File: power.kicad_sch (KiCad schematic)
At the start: 28 parts, among them Q1 CSD16340Q3, Q2 CSD17311Q5, U10 DS4432U+, U8 INA260, U9 TPS40305

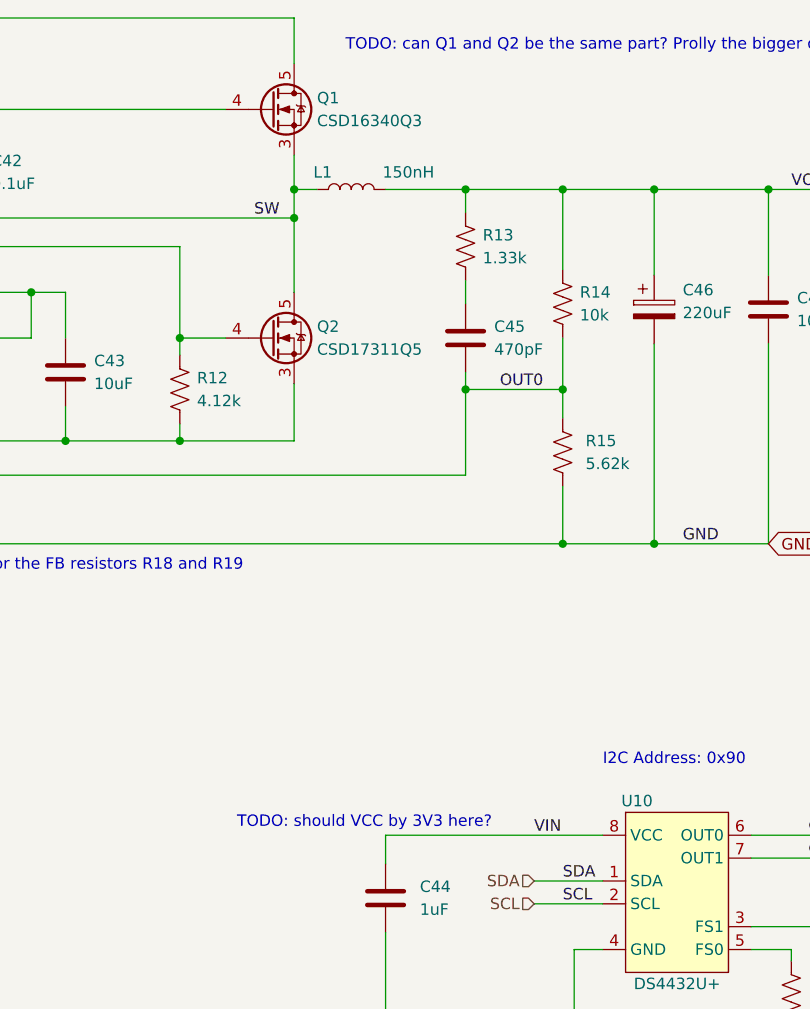
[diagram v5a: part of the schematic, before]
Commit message: schematic done, all footprints added, 3D files added. Rough placement done. needs lots of routing.
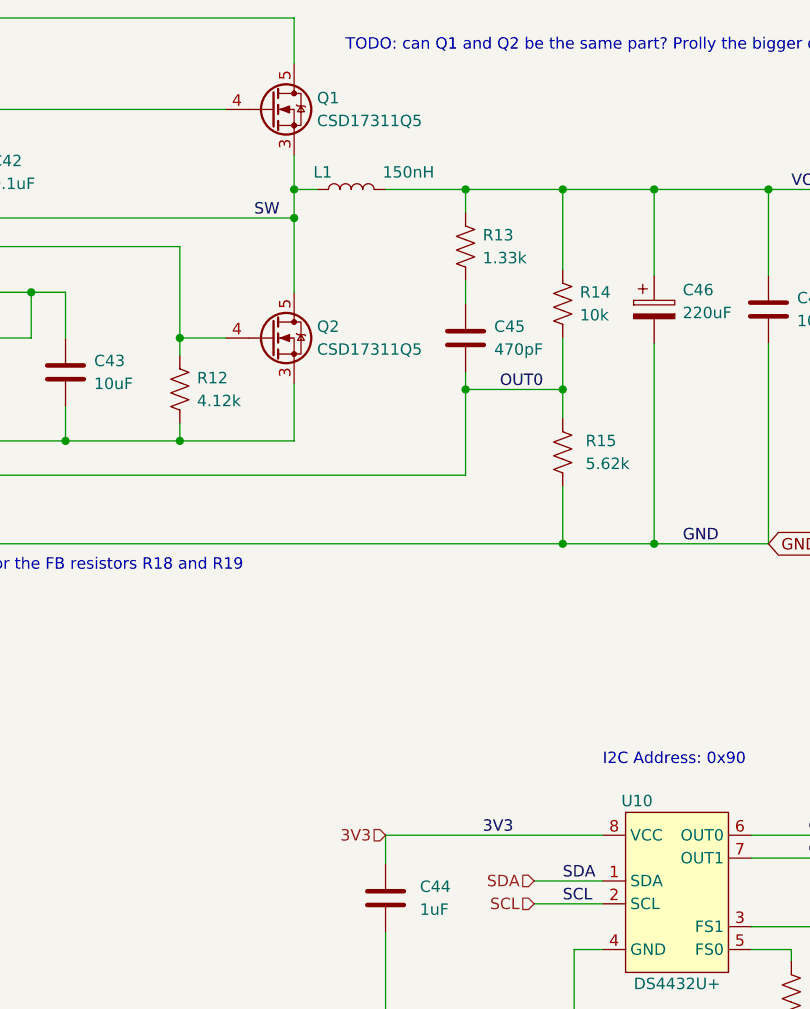
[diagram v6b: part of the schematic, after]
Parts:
- C35, C44: footprint Capacitor_SMD:C_0805_2012Metric -> Capacitor_SMD:C_0402_1005Metric
- Q1: value CSD16340Q3 -> CSD17311Q5; footprint TPS40305_supply:CSD16340Q3 -> TPS40305_supply:CSD17311Q5; DK 296-25646-1-ND -> 296-27625-1-ND; PARTNO CSD16340Q3 -> CSD17311Q5
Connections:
- net 3V3: now also C44.1, U10.8 (VCC)
- net VIN: no longer C44.1, U10.8 (VCC)
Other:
- note removed: "TODO: should VCC by 3V3 here?"
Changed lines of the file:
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@@
-    (effects (font (size 1.27 1.27)) (justify left bottom))
-  )
-  (text "TODO: should VCC by 3V3 here?" (at 176.53 110.49 0)
     (effects (font (size 1.27 1.27)) (justify left bottom))
   )
@@
     (effects (font (size 1.27 1.27)) (justify left bottom))
   )
+  (label "3V3" (at 203.835 111.125 0)
+    (effects (font (size 1.27 1.27)) (justify left bottom))
+  )
   (label "SDA" (at 212.725 116.205 0)
     (effects (font (size 1.27 1.27)) (justify left bottom))
@@
   )
   (label "GND" (at 67.945 153.67 0)
-    (effects (font (size 1.27 1.27)) (justify left bottom))
-  )
-  (label "VIN" (at 209.55 111.125 0)
     (effects (font (size 1.27 1.27)) (justify left bottom))
   )
@@
   )
   (hierarchical_label "VIN" (shape input) (at 52.705 104.775 180)
+    (effects (font (size 1.27 1.27)) (justify right))
+  )
+  (hierarchical_label "3V3" (shape input) (at 193.04 111.125 180)
     (effects (font (size 1.27 1.27)) (justify right))
   )
@@
     (pin "5")
   )
-  (symbol (lib_id "TPS40305:Q_NMOS_CSD17311Q5") (at 180.34 30.48 0) (unit 1)
-    (in_bom yes) (on_board yes)
-    (property "Reference" "Q1" (id 0) (at 185.42 29.21 0)
-      (effects (font (size 1.27 1.27)) (justify left))
-    )
-    (property "Value" "CSD16340Q3" (id 1) (at 185.42 31.75 0)
-      (effects (font (size 1.27 1.27)) (justify left))
-    )
-    (property "Footprint" "TPS40305_supply:CSD16340Q3" (id 2) (at 185.42 27.94 0)
-      (effects (font (size 1.27 1.27)) hide)
-    )
-    (property "Datasheet" "https://www.ti.com/lit/ds/symlink/csd16340q3.pdf" (id 3) (at 180.34 30.48 0)
-      (effects (font (size 1.27 1.27)) hide)
-    )
-    (property "PARTNO" "CSD16340Q3" (id 4) (at 180.34 30.48 0)
-      (effects (font (size 1.27 1.27)) hide)
-    )
-    (property "DK" "296-25646-1-ND" (id 5) (at 180.34 30.48 0)
-      (effects (font (size 1.27 1.27)) hide)
-    )
-    (pin "1")
-    (pin "2")
-    (pin "3")
-    (pin "4")
-    (pin "5")
-  )
   (symbol (lib_id "Device:C") (at 85.09 40.64 0) (unit 1)
     (in_bom yes) (on_board yes) (fields_autoplaced)
@@
       (effects (font (size 1.27 1.27)) (justify left))
     )
-    (property "Footprint" "Capacitor_SMD:C_0805_2012Metric" (id 2) (at 194.0052 121.92 0)
+    (property "Footprint" "Capacitor_SMD:C_0402_1005Metric" (id 2) (at 194.0052 121.92 0)
       (effects (font (size 1.27 1.27)) hide)
     )
@@
     (pin "1")
     (pin "2")
+  )
+  (symbol (lib_name "Q_NMOS_CSD17311Q5_1") (lib_id "TPS40305:Q_NMOS_CSD17311Q5") (at 180.34 30.48 0) (unit 1)
+    (in_bom yes) (on_board yes)
+    (property "Reference" "Q1" (id 0) (at 185.42 29.21 0)
+      (effects (font (size 1.27 1.27)) (justify left))
+    )
+    (property "Value" "CSD17311Q5" (id 1) (at 185.42 31.75 0)
+      (effects (font (size 1.27 1.27)) (justify left))
+    )
+    (property "Footprint" "TPS40305_supply:CSD17311Q5" (id 2) (at 185.42 27.94 0)
+      (effects (font (size 1.27 1.27)) hide)
+    )
+    (property "Datasheet" "https://www.ti.com/lit/ds/symlink/csd17311q5.pdf" (id 3) (at 180.34 30.48 0)
+      (effects (font (size 1.27 1.27)) hide)
+    )
+    (property "DK" "296-27625-1-ND" (id 4) (at 180.34 30.48 0)
+      (effects (font (size 1.27 1.27)) hide)
+    )
+    (property "PARTNO" "CSD17311Q5" (id 5) (at 180.34 30.48 0)
+      (effects (font (size 1.27 1.27)) hide)
+    )
+    (pin "1")
+    (pin "2")
+    (pin "3")
+    (pin "4")
+    (pin "5")
   )
   (symbol (lib_id "Device:C") (at 201.93 55.88 0) (unit 1)
@@
       (effects (font (size 1.27 1.27)) (justify left))
     )
-    (property "Footprint" "Capacitor_SMD:C_0805_2012Metric" (id 2) (at 46.0502 140.335 0)
-      (effects (font (size 1.27 1.27)) hide)
-    )
+    (property "Footprint" "Capacitor_SMD:C_0402_1005Metric" (id 2) (at 46.0502 140.335 0)
+      (effects (font (size 1.27 1.27)) hide)
+    )

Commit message: added almost all of the feedback from NebulaMiner
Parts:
- added R4: 10K, Resistor_SMD:R_0402_1005Metric, symbol Device:R_US
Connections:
- net 3V3: now also R4.1
- net PGOOD: now reaches R11.1, U9.3 (PGOOD)
- net PGOOD: now also R4.2
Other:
- moved on the sheet: R11
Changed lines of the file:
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@@
 (kicad_sch (version 20211123) (generator eeschema)
   (paper "A4")
+  (junction (at 135.89 116.84) (diameter 0) (color 0 0 0 0)
+  )
   (junction (at 62.865 50.165) (diameter 0) (color 0 0 0 0)
   )
@@
     (stroke (width 0) (type default) (color 0 0 0 0))
   )
+  (wire (pts (xy 124.46 116.84) (xy 135.89 116.84))
+    (stroke (width 0) (type default) (color 0 0 0 0))
+  )
   (wire (pts (xy 87.63 71.12) (xy 87.63 64.77))
     (stroke (width 0) (type default) (color 0 0 0 0))
@@
     (stroke (width 0) (type default) (color 0 0 0 0))
   )
-  (wire (pts (xy 146.685 50.8) (xy 153.67 50.8))
+  (wire (pts (xy 152.4 50.8) (xy 153.67 50.8))
     (stroke (width 0) (type default) (color 0 0 0 0))
   )
@@
     (stroke (width 0) (type default) (color 0 0 0 0))
   )
+  (wire (pts (xy 135.89 116.84) (xy 146.685 116.84))
+    (stroke (width 0) (type default) (color 0 0 0 0))
+  )
   (wire (pts (xy 170.18 55.88) (xy 170.18 57.785))
     (stroke (width 0) (type default) (color 0 0 0 0))
@@
     (stroke (width 0) (type default) (color 0 0 0 0))
   )
-  (wire (pts (xy 135.255 50.8) (xy 139.065 50.8))
+  (wire (pts (xy 135.255 50.8) (xy 144.78 50.8))
     (stroke (width 0) (type default) (color 0 0 0 0))
   )
@@
     (stroke (width 0) (type default) (color 0 0 0 0))
   )
+  (wire (pts (xy 135.89 114.3) (xy 135.89 116.84))
+    (stroke (width 0) (type default) (color 0 0 0 0))
+  )
   (wire (pts (xy 62.865 47.625) (xy 62.865 50.165))
     (stroke (width 0) (type default) (color 0 0 0 0))
@@
   )
   (wire (pts (xy 182.88 39.37) (xy 185.42 39.37))
+    (stroke (width 0) (type default) (color 0 0 0 0))
+  )
+  (wire (pts (xy 135.89 100.33) (xy 135.89 106.68))
     (stroke (width 0) (type default) (color 0 0 0 0))
   )
@@
     (effects (font (size 1.27 1.27)) (justify left bottom))
   )
+  (label "PGOOD" (at 137.16 50.8 0)
+    (effects (font (size 1.27 1.27)) (justify left bottom))
+  )
   (label "GND" (at 45.085 144.145 0)
     (effects (font (size 1.27 1.27)) (justify left bottom))
@@
   )
   (label "GND" (at 223.52 137.795 0)
+    (effects (font (size 1.27 1.27)) (justify left bottom))
+  )
+  (label "3V3" (at 135.89 104.14 0)
+    (effects (font (size 1.27 1.27)) (justify left bottom))
+  )
+  (label "PGOOD" (at 127 116.84 0)
     (effects (font (size 1.27 1.27)) (justify left bottom))
   )
@@
   (hierarchical_label "3V3" (shape input) (at 193.04 111.125 180)
     (effects (font (size 1.27 1.27)) (justify right))
+  )
+  (hierarchical_label "PGOOD" (shape output) (at 146.685 116.84 0)
+    (effects (font (size 1.27 1.27)) (justify left))
   )
   (symbol (lib_id "Device:C") (at 157.48 59.69 0) (unit 1)
@@
     (pin "2")
   )
-  (symbol (lib_id "Device:R_US") (at 142.875 50.8 90) (unit 1)
+  (symbol (lib_id "Device:R_US") (at 148.59 50.8 90) (unit 1)
     (in_bom yes) (on_board yes)
-    (property "Reference" "R11" (id 0) (at 138.43 49.53 90))
-    (property "Value" "100k" (id 1) (at 147.32 49.53 90))
-    (property "Footprint" "Resistor_SMD:R_0402_1005Metric" (id 2) (at 143.129 49.784 90)
-      (effects (font (size 1.27 1.27)) hide)
-    )
-    (property "Datasheet" "~" (id 3) (at 142.875 50.8 0)
-      (effects (font (size 1.27 1.27)) hide)
-    )
-    (property "DK" "311-100KJRCT-ND" (id 4) (at 142.875 50.8 0)
+    (property "Reference" "R11" (id 0) (at 148.59 48.26 90))
+    (property "Value" "100k" (id 1) (at 148.59 53.34 90))
+    (property "Footprint" "Resistor_SMD:R_0402_1005Metric" (id 2) (at 148.844 49.784 90)
+      (effects (font (size 1.27 1.27)) hide)
+    )
+    (property "Datasheet" "~" (id 3) (at 148.59 50.8 0)
+      (effects (font (size 1.27 1.27)) hide)
+    )
+    (property "DK" "311-100KJRCT-ND" (id 4) (at 148.59 50.8 0)
       (effects (font (size 1.27 1.27)) hide)
     )
@@
       (effects (font (size 1.27 1.27)) hide)
     )
+    (pin "1")
+    (pin "2")
+  )
+  (symbol (lib_id "Device:R_US") (at 135.89 110.49 0) (unit 1)
+    (in_bom yes) (on_board yes) (fields_autoplaced)
+    (property "Reference" "R4" (id 0) (at 138.43 109.2199 0)
+      (effects (font (size 1.27 1.27)) (justify left))
+    )
+    (property "Value" "10K" (id 1) (at 138.43 111.7599 0)
+      (effects (font (size 1.27 1.27)) (justify left))
+    )
+    (property "Footprint" "Resistor_SMD:R_0402_1005Metric" (id 2) (at 136.906 110.744 90)
+      (effects (font (size 1.27 1.27)) hide)
+    )
+    (property "Datasheet" "~" (id 3) (at 135.89 110.49 0)
+      (effects (font (size 1.27 1.27)) hide)
+    )
+    (property "DK" "YAG1346CT-ND" (id 4) (at 135.89 110.49 0)
+      (effects (font (size 1.27 1.27)) hide)
+    )

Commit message: part library cleanup
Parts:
- C35, C44: DK 1276-6471-1-ND -> 587-5514-1-ND
- C42: DK 1276-1043-1-ND -> 1292-1639-1-ND
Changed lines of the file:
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@@
       (effects (font (size 1.27 1.27)) hide)
     )
-    (property "Datasheet" "~" (id 3) (at 157.48 59.69 0)
+    (property "Datasheet" "" (id 3) (at 157.48 59.69 0)
       (effects (font (size 1.27 1.27)) hide)
     )
@@
       (effects (font (size 1.27 1.27)) hide)
     )
-    (property "Datasheet" "~" (id 3) (at 145.415 37.465 0)
-      (effects (font (size 1.27 1.27)) hide)
-    )
-    (property "DK" "1276-1043-1-ND" (id 4) (at 145.415 37.465 0)
+    (property "Datasheet" "" (id 3) (at 145.415 37.465 0)
+      (effects (font (size 1.27 1.27)) hide)
+    )
+    (property "DK" "1292-1639-1-ND" (id 4) (at 145.415 37.465 0)
       (effects (font (size 1.27 1.27)) hide)
     )
@@
       (effects (font (size 1.27 1.27)) hide)
     )
-    (property "Datasheet" "~" (id 3) (at 193.04 118.11 0)
-      (effects (font (size 1.27 1.27)) hide)
-    )
-    (property "DK" "1276-6471-1-ND" (id 4) (at 193.04 118.11 0)
+    (property "Datasheet" "" (id 3) (at 193.04 118.11 0)
+      (effects (font (size 1.27 1.27)) hide)
+    )
+    (property "DK" "587-5514-1-ND" (id 4) (at 193.04 118.11 0)
       (effects (font (size 1.27 1.27)) hide)
     )
@@
       (effects (font (size 1.27 1.27)) hide)
     )
-    (property "Datasheet" "~" (id 3) (at 45.085 136.525 0)
-      (effects (font (size 1.27 1.27)) hide)
-    )
-    (property "DK" "1276-6471-1-ND" (id 4) (at 45.085 136.525 0)
-      (effects (font (size 1.27 1.27)) hide)
-    )
+    (property "Datasheet" "" (id 3) (at 45.085 136.525 0)
+      (effects (font (size 1.27 1.27)) hide)
+    )
+    (property "DK" "587-5514-1-ND" (id 4) (at 45.085 136.525 0)
+      (effects (font (size 1.27 1.27)) hide)
+    )
